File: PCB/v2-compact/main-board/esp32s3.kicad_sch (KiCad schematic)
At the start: 0 parts

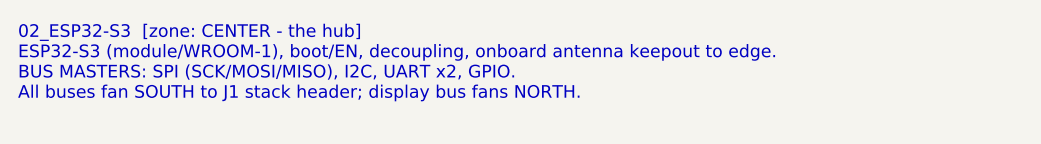
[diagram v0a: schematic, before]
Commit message: PCB: rework main board to phone-style layout; J1 -> horizontal strip
Main board (per feedback) is now a phone-style split — front is pure UI, back
carries the electronics:
- FRONT: status LEDs at the very top (above the display), TFT rotated to
  LANDSCAPE (sideways), nav buttons below it and moved down. Same feel as the
  ESP32-DIV, sideways screen.
- BACK: ESP32-S3 behind the display, microSD beside it, power + USB-C at the
  bottom-centre edge like a phone.

To keep the centre column free for the landscape display and the bottom-centre
USB-C, J1 is reoriented from a vertical 2x10 to a HORIZONTAL 10x2 strip in the
lower-centre. J1 is the shared mating datum, so the shield's J1 moves to match;
the shield's RV1106 / HTRC110 / bulk-cap zones shift to sit above/below the new
strip (SPI spine still runs north from it). Every v1 capability unchanged.

Updated both .kicad_pcb, both floorplan SVGs, both schematics' zone specs, and
PLACEMENT.md. Verified: files parse, J1 clears all zones, no same-side overlaps.

Co-Authored-By: Claude <noreply@anthropic.com>
Claude-Session: https://claude.ai/code/session_017BEAKBRVwbUCc7Sa2o3Ye7
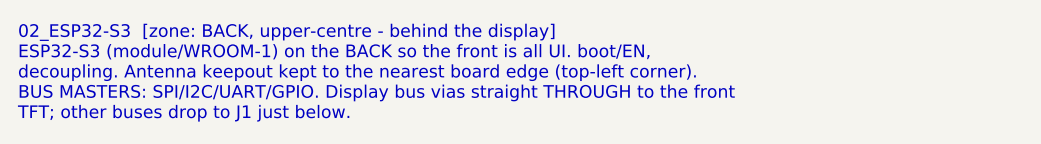
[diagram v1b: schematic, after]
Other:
- note added: "02_ESP32-S3 [zone: BACK, upper-centre - behind the display] ESP32-S3 (module/WROOM-1) on the BACK so the front is all UI. boot/EN, decoupling. Antenna keepout kept to the nearest board edge (top-left corner). BUS MASTERS: SPI/I2C/UART/GPIO. Display bus vias straight THROUGH to the front TFT; other buses drop to J1 just below."
- note removed: "02_ESP32-S3 [zone: CENTER - the hub] ESP32-S3 (module/WROOM-1), boot/EN, decoupling, onboard antenna keepout to edge. BUS MASTERS: SPI (SCK/MOSI/MISO), I2C, UART x2, GPIO. All buses fan SOUTH to J1 stack header; display bus fans NORTH."
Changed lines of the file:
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@@
   (paper "A4")
   (title_block (title "02_ESP32-S3") (company "YurilLAB"))
-  (text "02_ESP32-S3  [zone: CENTER - the hub]
-ESP32-S3 (module/WROOM-1), boot/EN, decoupling, onboard antenna keepout to edge.
-BUS MASTERS: SPI (SCK/MOSI/MISO), I2C, UART x2, GPIO.
-All buses fan SOUTH to J1 stack header; display bus fans NORTH." (at 15 15 0)
+  (text "02_ESP32-S3  [zone: BACK, upper-centre - behind the display]
+ESP32-S3 (module/WROOM-1) on the BACK so the front is all UI. boot/EN,
+decoupling. Antenna keepout kept to the nearest board edge (top-left corner).
+BUS MASTERS: SPI/I2C/UART/GPIO. Display bus vias straight THROUGH to the front
+TFT; other buses drop to J1 just below." (at 15 15 0)
     (effects (font (size 1.4 1.4)) (justify left top)))
   (sheet_instances (path "/" (page "1")))
